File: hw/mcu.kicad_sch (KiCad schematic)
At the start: 7 parts, among them J1 Prog/debug, U1 STM32L432KBUx

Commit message: WIP
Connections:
- net LCD_nSS: now reaches U1.10 (PA4)
- net LCD_SCK: now reaches U1.11 (PA5)
- net LCD_MISO: now reaches U1.12 (PA6)
- net LCD_MOSI: now reaches U1.13 (PA7)
- net USB_DM: now reaches U1.21 (PA11)
- net USB_DP: now reaches U1.22 (PA12)
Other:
- note added: "SPI1"
- note added: "TODO: 32 kHz crystal"
- note added: "TODO: LCD"
- note added: "TODO: maybe add a QSPI flash?"
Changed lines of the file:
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@@
+		)
+	)
+	(text "SPI1"
+		(exclude_from_sim no)
+		(at 156.464 86.868 0)
+		(effects
+			(font
+				(size 1.27 1.27)
+			)
+		)
+	)
+	(text "TODO: 32 kHz crystal"
+		(exclude_from_sim no)
+		(at 98.806 85.09 0)
+		(effects
+			(font
+				(size 1.27 1.27)
+			)
 		)
 	)
@@
 		)
 	)
+	(text "TODO: maybe add a QSPI flash?"
+		(exclude_from_sim no)
+		(at 121.158 145.288 0)
+		(effects
+			(font
+				(size 1.27 1.27)
+			)
+		)
+	)
+	(text "TODO: LCD"
+		(exclude_from_sim no)
+		(at 77.216 157.988 0)
+		(effects
+			(font
+				(size 1.27 1.27)
+			)
+		)
+	)
 	(junction
 		(at 149.86 53.34)
@@
 	(wire
 		(pts
+			(xy 135.89 88.9) (xy 149.86 88.9)
+		)
+		(stroke
+			(width 0)
+			(type default)
+		)
+	)
+	(wire
+		(pts
+			(xy 135.89 91.44) (xy 149.86 91.44)
+		)
+		(stroke
+			(width 0)
+			(type default)
+		)
+	)
+	(wire
+		(pts
 			(xy 102.87 73.66) (xy 110.49 73.66)
 		)
@@
 	(wire
 		(pts
+			(xy 135.89 101.6) (xy 149.86 101.6)
+		)
+		(stroke
+			(width 0)
+			(type default)
+		)
+	)
+	(wire
+		(pts
+			(xy 135.89 104.14) (xy 149.86 104.14)
+		)
+		(stroke
+			(width 0)
+			(type default)
+		)
+	)
+	(wire
+		(pts
 			(xy 144.78 53.34) (xy 149.86 53.34)
 		)
@@
 	(wire
 		(pts
+			(xy 135.89 83.82) (xy 149.86 83.82)
+		)
+		(stroke
+			(width 0)
+			(type default)
+		)
+	)
+	(wire
+		(pts
 			(xy 130.81 53.34) (xy 139.7 53.34)
 		)
@@
 		(pts
 			(xy 120.65 66.04) (xy 123.19 66.04)
+		)
+		(stroke
+			(width 0)
+			(type default)
+		)
+	)
+	(wire
+		(pts
+			(xy 135.89 86.36) (xy 149.86 86.36)
 		)
 		(stroke
@@
 		)
 	)
+	(label "LCD_MISO"
+		(at 78.74 168.91 180)
+		(effects
+			(font
+				(size 1.27 1.27)
+			)
+			(justify right bottom)
+		)
+	)
+	(label "LCD_nSS"
+		(at 78.74 163.83 180)
+		(effects
+			(font
+				(size 1.27 1.27)
+			)
+			(justify right bottom)
+		)
+	)
 	(label "nRST"
 		(at 241.3 119.38 0)
@@
 		)
 	)
+	(label "LCD_MISO"
+		(at 149.86 88.9 180)
+		(effects
+			(font
+				(size 1.27 1.27)
+			)
+			(justify right bottom)
+		)
+	)
+	(label "LCD_MOSI"
+		(at 149.86 91.44 180)
+		(effects
+			(font
+				(size 1.27 1.27)
+			)
+			(justify right bottom)
+		)
+	)
+	(label "LCD_SCK"
+		(at 149.86 86.36 180)
+		(effects
+			(font
+				(size 1.27 1.27)
+			)
+			(justify right bottom)
+		)
+	)
 	(label "SWCLK"
 		(at 144.78 109.22 180)
@@
 		)
 	)
+	(label "LCD_MOSI"
+		(at 78.74 171.45 180)
+		(effects
+			(font
+				(size 1.27 1.27)
+			)
+			(justify right bottom)
+		)
+	)
+	(label "LCD_nSS"
+		(at 149.86 83.82 180)
+		(effects
+			(font
+				(size 1.27 1.27)
+			)
+			(justify right bottom)
+		)
+	)
+	(label "LCD_SCK"
+		(at 78.74 166.37 180)
+		(effects
+			(font
+				(size 1.27 1.27)
+			)
+			(justify right bottom)
+		)
+	)
+	(hierarchical_label "USB_DM"
+		(shape bidirectional)
+		(at 149.86 101.6 0)
+		(effects
+			(font
+				(size 1.27 1.27)
+			)
+			(justify left)
+		)
+	)
+	(hierarchical_label "USB_DP"
+		(shape bidirectional)
+		(at 149.86 104.14 0)
+		(effects
+			(font
+				(size 1.27 1.27)
+			)
+			(justify left)
+		)
+	)

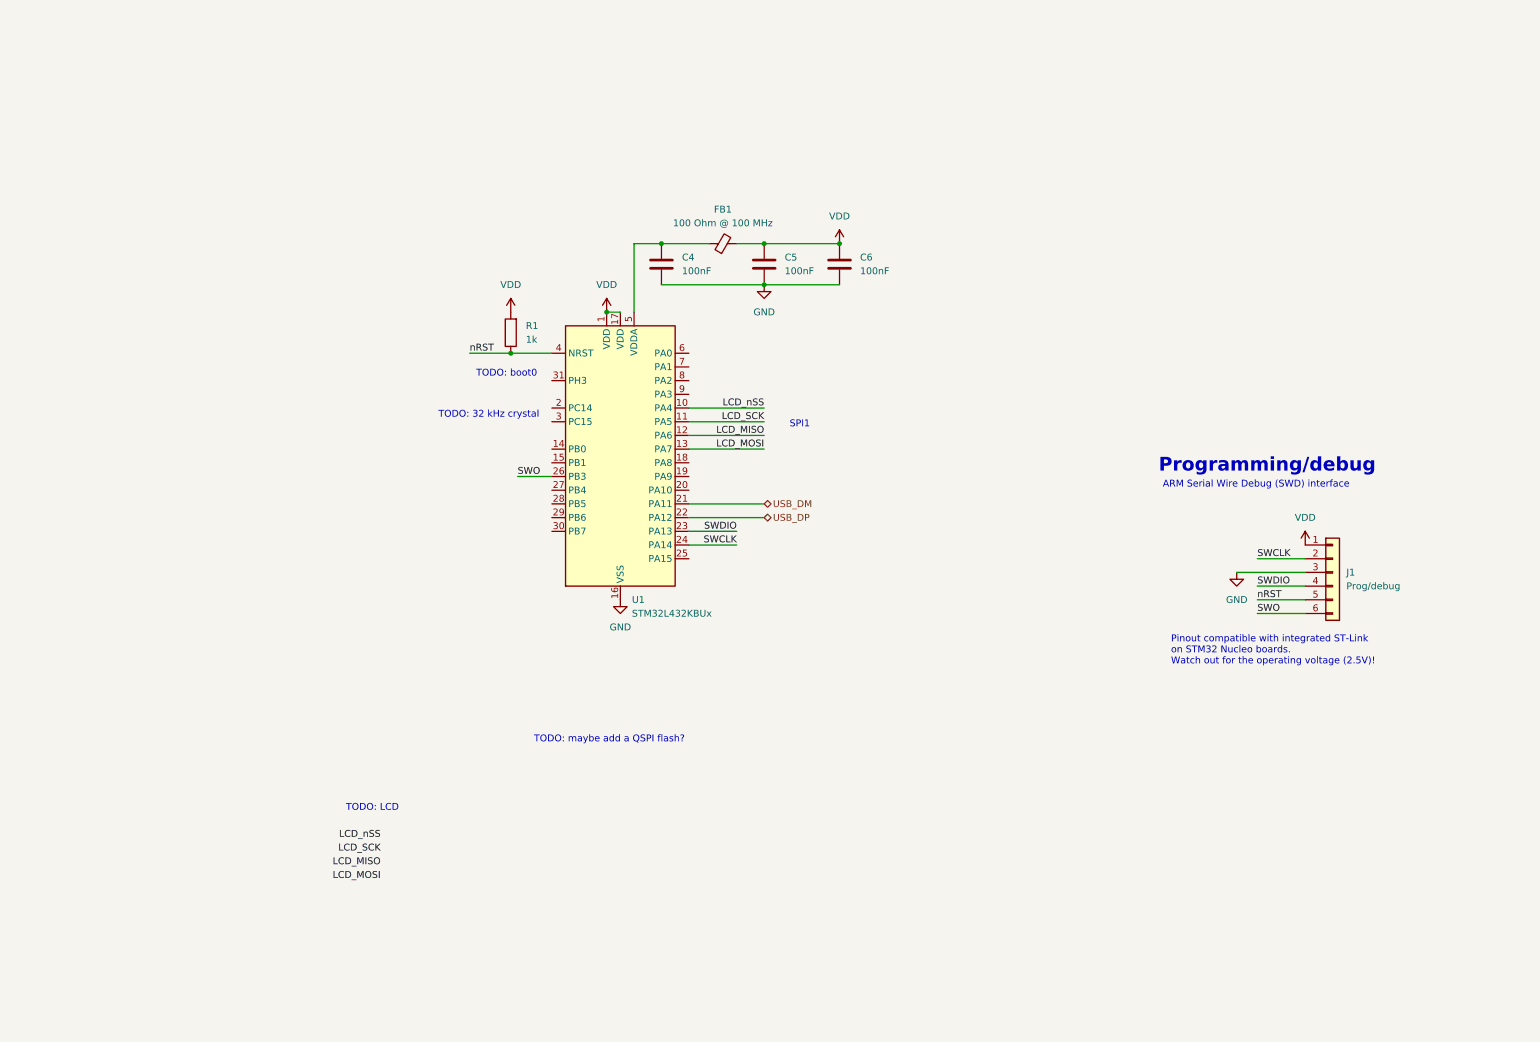
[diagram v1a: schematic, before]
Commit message: Added different voltage regulator.
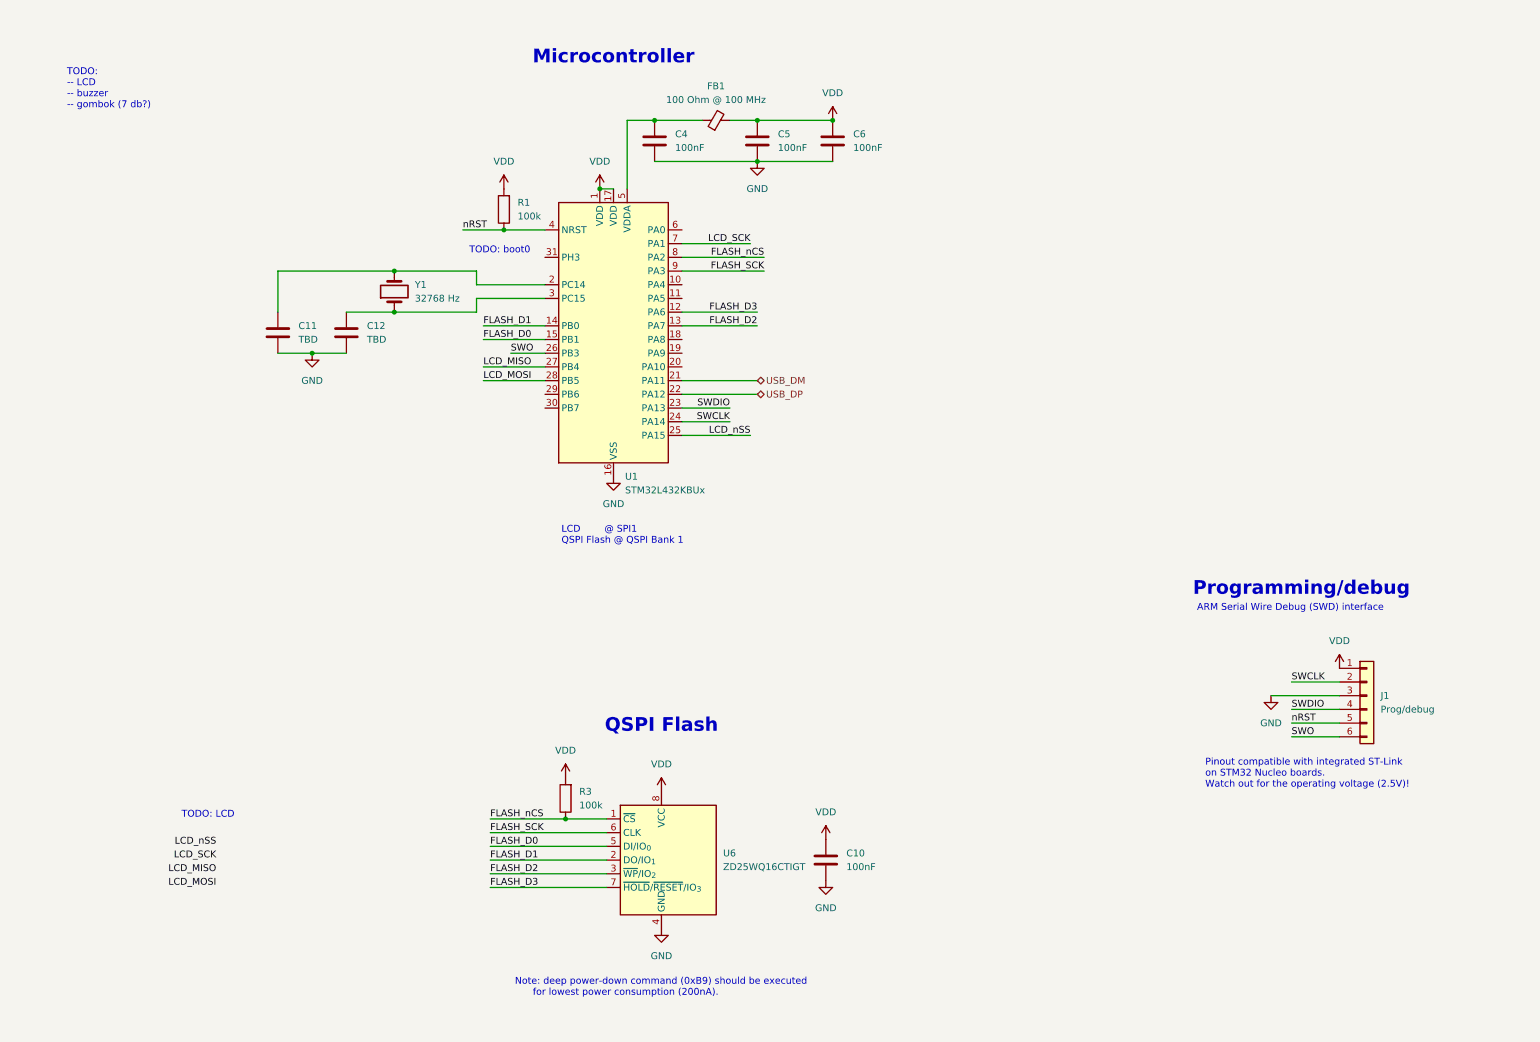
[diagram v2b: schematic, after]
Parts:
- added C10: 100nF, Capacitor_SMD:C_0805_2012Metric, symbol Device:C
- added C11, C12: TBD, Capacitor_SMD:C_0805_2012Metric, symbol Device:C
- added R3: 100k, Resistor_SMD:R_0805_2012Metric, symbol Device:R
- added U6: ZD25WQ16CTIGT, Package_SO:SOIC-8_3.9x4.9mm_P1.27mm, symbol Memory_Flash:W25Q32JVSS
- added Y1: 32768 Hz, symbol Device:Crystal
- R1: value 1k -> 100k
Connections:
- net GND: now also C10.1, C11.1, C12.1, U6.4 (GND)
- net LCD_MISO: now also U1.27 (PB4); no longer U1.12 (PA6)
- net LCD_MOSI: now also U1.28 (PB5); no longer U1.13 (PA7)
- net LCD_SCK: now also U1.7 (PA1); no longer U1.11 (PA5)
- net LCD_nSS: now also U1.25 (PA15); no longer U1.10 (PA4)
- net VDD: now also C10.2, R3.2, U6.8 (VCC)
- net FLASH_D1: now reaches U1.14 (PB0)
- net FLASH_D1: now also U6.2 (DO/IO_{1})
- net FLASH_D0: now reaches U1.15 (PB1)
- net FLASH_D0: now also U6.5 (DI/IO_{0})
- net at U1.2 (PC14): now also C11.2, Y1.2
- net at U1.3 (PC15): now also C12.2, Y1.1
- net FLASH_nCS: now reaches U1.8 (PA2)
- net FLASH_nCS: now also R3.1, U6.1 (~{CS})
- net FLASH_SCK: now reaches U1.9 (PA3)
- net FLASH_SCK: now also U6.6 (CLK)
- new net FLASH_D2: U1.13 (PA7), U6.3 (~{WP}/IO_{2})
- new net FLASH_D3: U1.12 (PA6), U6.7 (~{HOLD}/~{RESET}/IO_{3})
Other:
- note added: "LCD @ SPI1 QSPI Flash @ QSPI Bank 1"
- note added: "Microcontroller"
- note added: "Note: deep power-down command (0xB9) should be executed for lowest power consumption (200nA)."
- note added: "QSPI Flash"
- note added: "TODO: -- LCD -- buzzer -- gombok (7 db?)"
- note removed: "SPI1"
- note removed: "TODO: 32 kHz crystal"
- note removed: "TODO: maybe add a QSPI flash?"
- moved on the sheet: C4, C5, C6, FB1, J1, R1, U1

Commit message: WIP
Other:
- note added: "TODO: csatlakoztatni"
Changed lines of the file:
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@@
+		)
+	)
+	(text "TODO: csatlakoztatni"
+		(exclude_from_sim no)
+		(at 167.386 68.58 0)
+		(effects
+			(font
+				(size 1.27 1.27)
+			)
 		)
 	)
@@
 		)
 	)
+	(label "LCD_nRST"
+		(at 172.72 74.93 180)
+		(effects
+			(font
+				(size 1.27 1.27)
+			)
+			(justify right bottom)
+		)
+	)
 	(label "SWCLK"
 		(at 247.65 134.62 0)
@@
 		)
 	)
+	(label "LCD_nRST"
+		(at 48.26 177.8 180)
+		(effects
+			(font
+				(size 1.27 1.27)
+			)
+			(justify right bottom)
+		)
+	)
+	(label "LCD_BL"
+		(at 172.72 77.47 180)
+		(effects
+			(font
+				(size 1.27 1.27)
+			)
+			(justify right bottom)
+		)
+	)
 	(label "nRST"
 		(at 93.98 50.8 0)
@@
 		)
 	)
+	(label "LCD_DC"
+		(at 172.72 72.39 180)
+		(effects
+			(font
+				(size 1.27 1.27)
+			)
+			(justify right bottom)
+		)
+	)
 	(label "FLASH_D3"
 		(at 148.59 66.04 180)
@@
 		)
 	)
+	(label "LCD_BL"
+		(at 48.26 180.34 180)
+		(effects
+			(font
+				(size 1.27 1.27)
+			)
+			(justify right bottom)
+		)
+	)
 	(label "FLASH_D0"
 		(at 97.79 71.12 0)
@@
 		)
 	)
+	(label "LCD_DC"
+		(at 48.26 175.26 180)
+		(effects
+			(font
+				(size 1.27 1.27)
+			)
+			(justify right bottom)
+		)
+	)
